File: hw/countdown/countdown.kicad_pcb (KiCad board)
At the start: 4 copper layers, 44 x 23 mm, 24 parts, among them J1 TC2030-SWD, SW1 TS-1187A-B-A-B, U1 STM32L031G6U6, Y1 32.768kHz

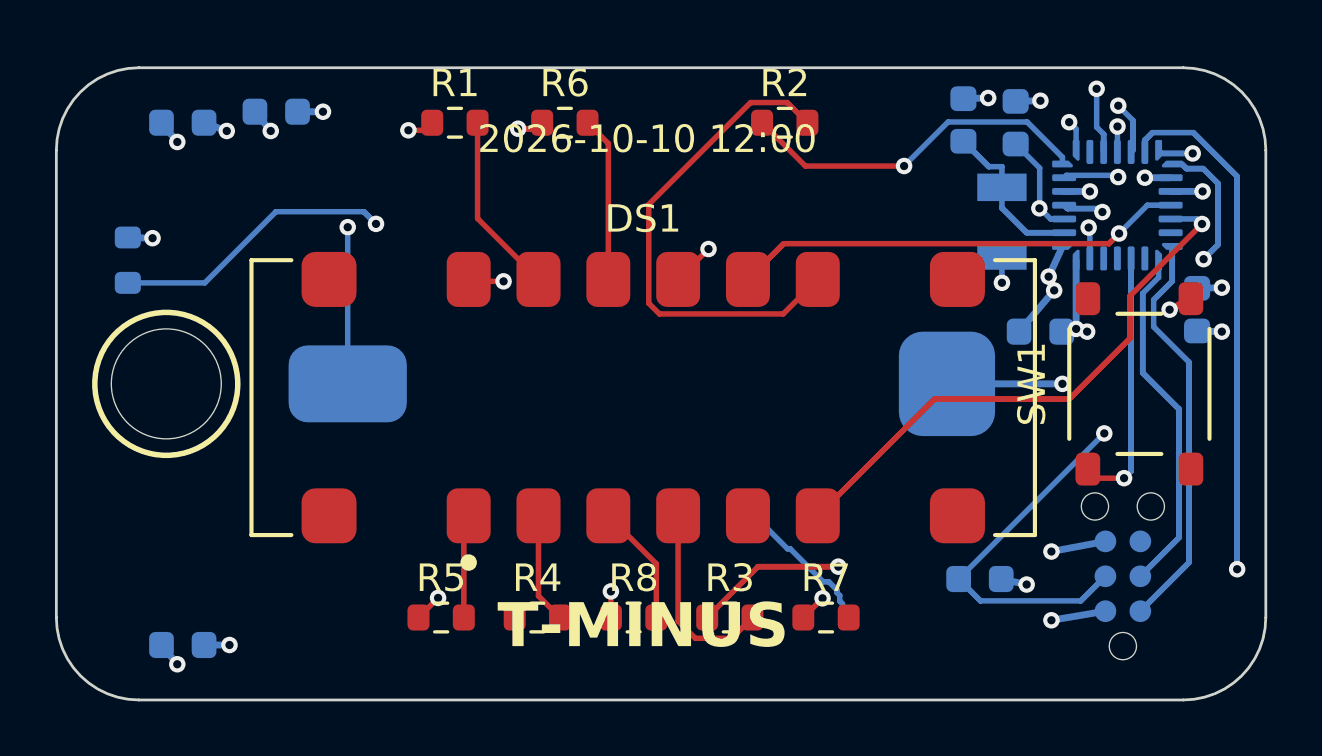
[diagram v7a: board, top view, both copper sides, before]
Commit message: Footprint/DFM review fixes: GND-only vias under QFN, via spacing gates, plated GND keyring ring, display pads to true terminal width, silk cleanup + hidden refs
Co-Authored-By: Claude Fable 5 <noreply@anthropic.com>
Claude-Session: https://claude.ai/code/session_01EyK7WVGPpPEnSjWLWWV8on
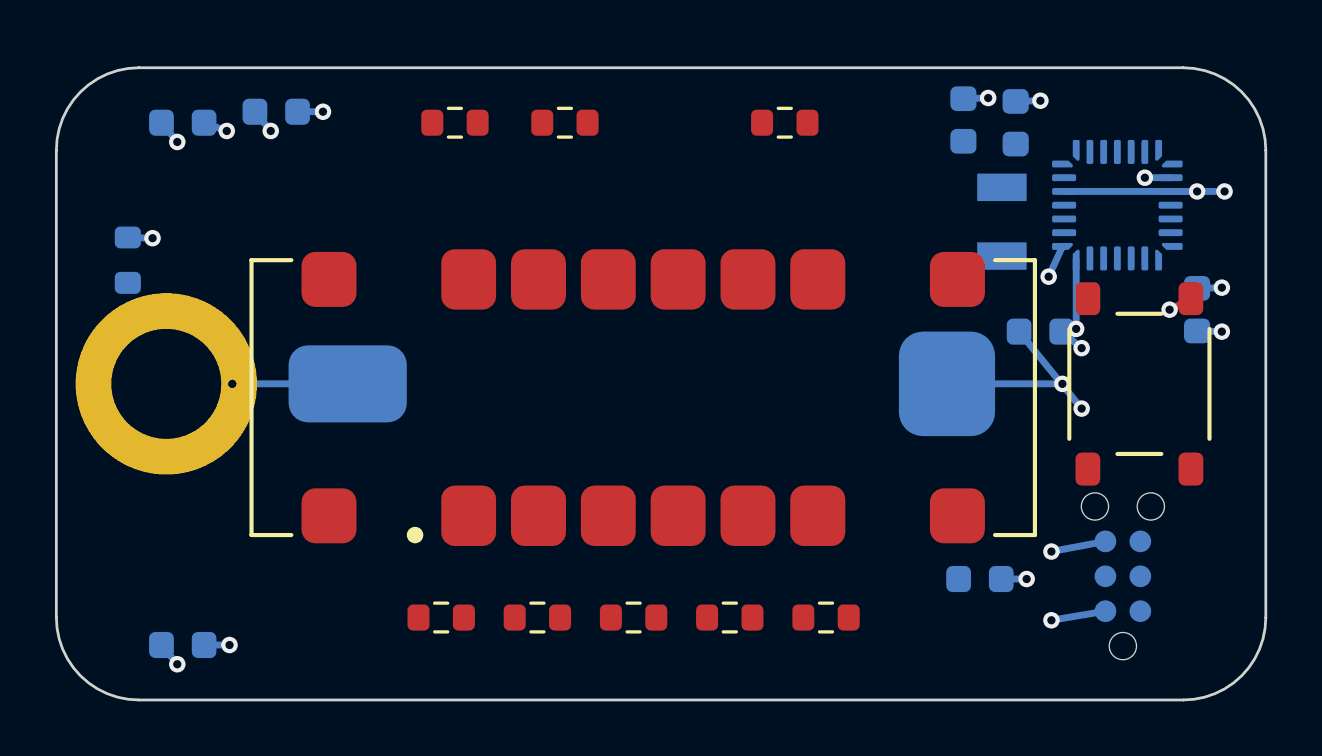
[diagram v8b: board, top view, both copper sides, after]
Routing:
- net GND: track 164.1 -> 19.6 mm, vias 14 -> 15
- net VDD: track 158.6 -> 21.4 mm
- net SEG_DP: track 83.0 -> 0.00 mm, vias 2 -> 0
- net SEG_E: track 66.2 -> 0.00 mm, vias 2 -> 0
- net BOOT0: track 63.9 -> 0.00 mm, vias 2 -> 0
- net SEG_G: track 54.1 -> 0.00 mm, vias 2 -> 0
- net DIG_1: track 52.9 -> 0.00 mm, vias 2 -> 0
- net SEG_F: track 46.2 -> 0.00 mm, vias 2 -> 0
- net SEG_C: track 41.1 -> 0.00 mm, vias 2 -> 0
- net NRST: track 36.6 -> 0.00 mm, vias 2 -> 0
- net DIG_4: track 36.1 -> 0.00 mm, vias 1 -> 0
- net SEG_A: track 30.0 -> 0.00 mm, vias 2 -> 0
- net DIG_2: track 29.2 -> 0.00 mm, vias 2 -> 0
- net SWDIO: track 26.8 -> 0.00 mm
- net SWCLK: track 24.3 -> 0.00 mm
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- removed copper zone on In1.Cu, net GND
- removed copper zone on In2.Cu, net VDD
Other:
- board text removed: "2026-10-10 12:00"
- board text removed: "COUNTDOWN v1 2026"
- board text removed: "T-MINUS"
